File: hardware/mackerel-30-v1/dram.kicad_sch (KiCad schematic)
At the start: 28 parts, among them J11 Conn_02x05_Odd_Even, U13 EPM7128, U14 SIMM72, U15 74ABT245, U16 74ABT245, U17 74ABT245, U2 74ABT245

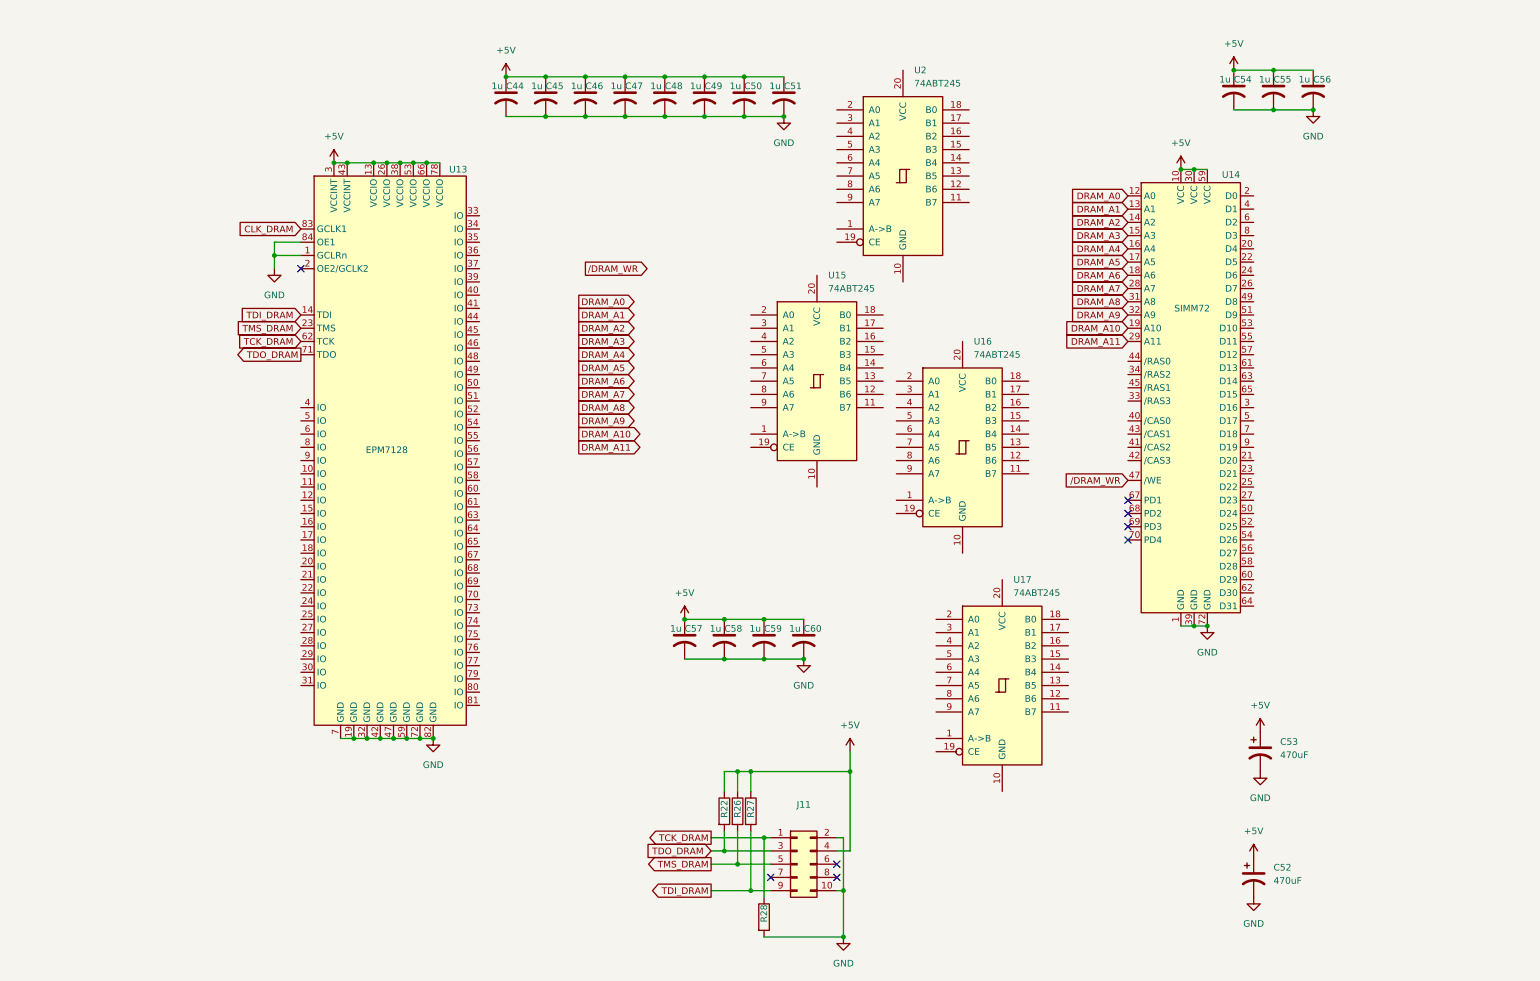
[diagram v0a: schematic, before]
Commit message: SIMM and data buffers mostly routed
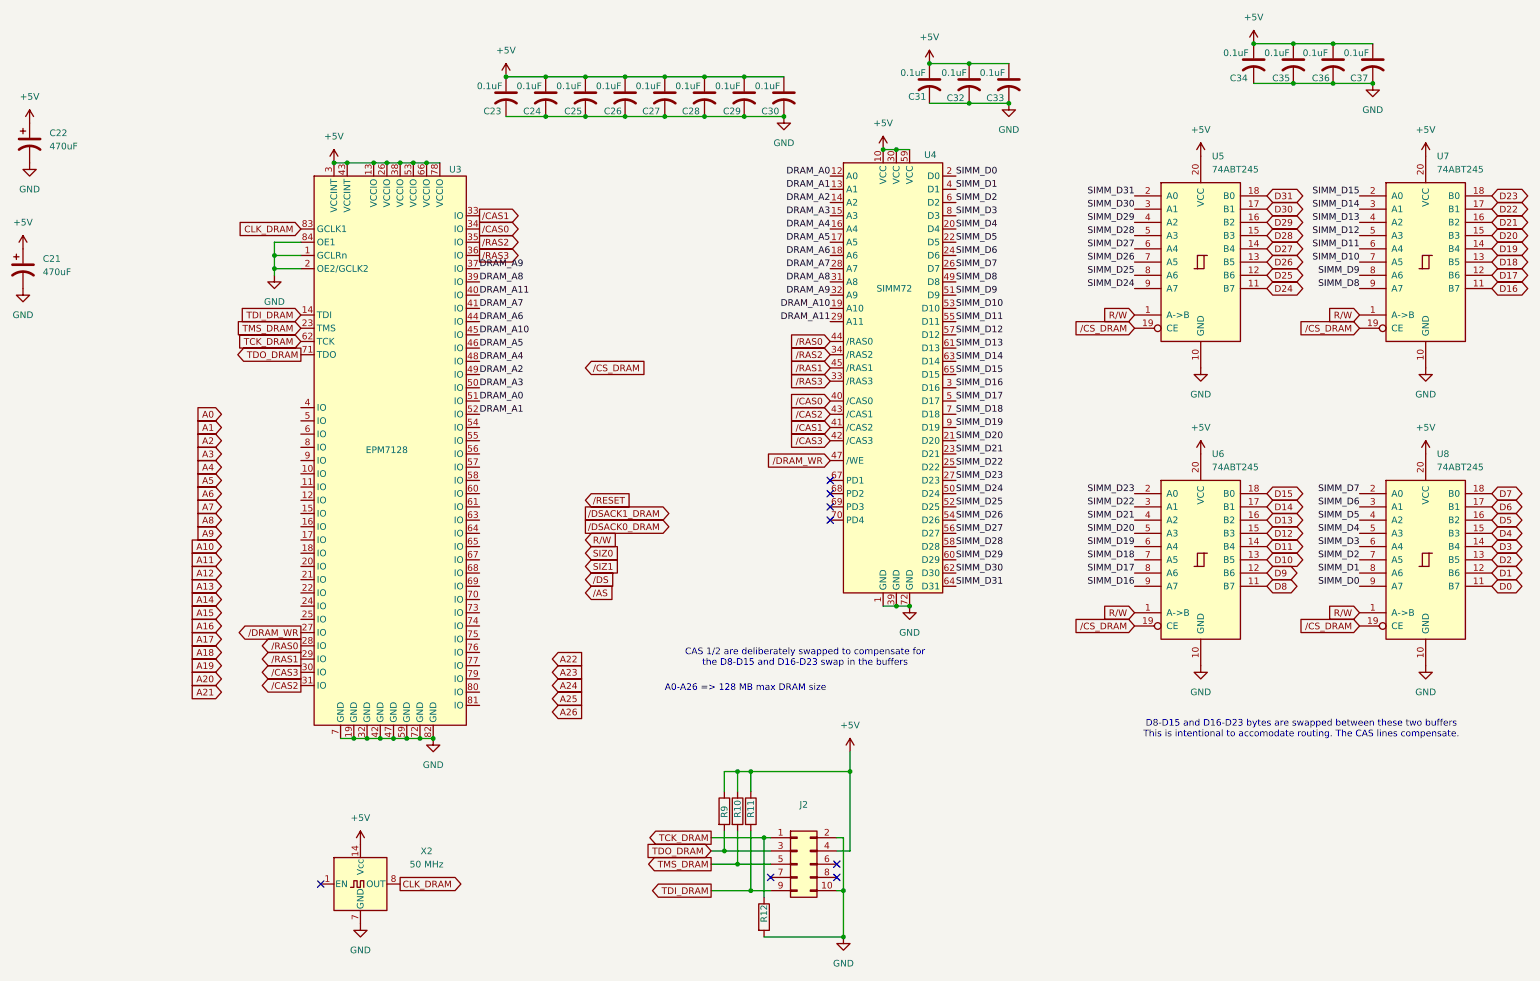
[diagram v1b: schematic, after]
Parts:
- added X2: 50 MHz, Oscillator:Oscillator_DIP-14, symbol Oscillator:CXO_DIP14
- C23: renamed from C44; value 1u -> 0.1uF; footprint Capacitor_SMD:C_0805_2012Metric_Pad1.18x1.45mm_HandSolder -> Capacitor_SMD:C_1206_3216Metric_Pad1.33x1.80mm_HandSolder
- C24: renamed from C45; value 1u -> 0.1uF; footprint Capacitor_SMD:C_0805_2012Metric_Pad1.18x1.45mm_HandSolder -> Capacitor_SMD:C_1206_3216Metric_Pad1.33x1.80mm_HandSolder
- C25: renamed from C46; value 1u -> 0.1uF; footprint Capacitor_SMD:C_0805_2012Metric_Pad1.18x1.45mm_HandSolder -> Capacitor_SMD:C_1206_3216Metric_Pad1.33x1.80mm_HandSolder
- C26: renamed from C47; value 1u -> 0.1uF; footprint Capacitor_SMD:C_0805_2012Metric_Pad1.18x1.45mm_HandSolder -> Capacitor_SMD:C_1206_3216Metric_Pad1.33x1.80mm_HandSolder
- C27: renamed from C48; value 1u -> 0.1uF; footprint Capacitor_SMD:C_0805_2012Metric_Pad1.18x1.45mm_HandSolder -> Capacitor_SMD:C_1206_3216Metric_Pad1.33x1.80mm_HandSolder
- C28: renamed from C49; value 1u -> 0.1uF; footprint Capacitor_SMD:C_0805_2012Metric_Pad1.18x1.45mm_HandSolder -> Capacitor_SMD:C_1206_3216Metric_Pad1.33x1.80mm_HandSolder
- C29: renamed from C50; value 1u -> 0.1uF; footprint Capacitor_SMD:C_0805_2012Metric_Pad1.18x1.45mm_HandSolder -> Capacitor_SMD:C_1206_3216Metric_Pad1.33x1.80mm_HandSolder
- C30: renamed from C51; value 1u -> 0.1uF; footprint Capacitor_SMD:C_0805_2012Metric_Pad1.18x1.45mm_HandSolder -> Capacitor_SMD:C_1206_3216Metric_Pad1.33x1.80mm_HandSolder
- C31: renamed from C54; value 1u -> 0.1uF; footprint Capacitor_SMD:C_0805_2012Metric_Pad1.18x1.45mm_HandSolder -> Capacitor_SMD:C_1206_3216Metric_Pad1.33x1.80mm_HandSolder
- C32: renamed from C55; value 1u -> 0.1uF; footprint Capacitor_SMD:C_0805_2012Metric_Pad1.18x1.45mm_HandSolder -> Capacitor_SMD:C_1206_3216Metric_Pad1.33x1.80mm_HandSolder
- C33: renamed from C56; value 1u -> 0.1uF; footprint Capacitor_SMD:C_0805_2012Metric_Pad1.18x1.45mm_HandSolder -> Capacitor_SMD:C_1206_3216Metric_Pad1.33x1.80mm_HandSolder
- C34: renamed from C57; value 1u -> 0.1uF; footprint Capacitor_SMD:C_0805_2012Metric_Pad1.18x1.45mm_HandSolder -> Capacitor_SMD:C_1206_3216Metric_Pad1.33x1.80mm_HandSolder
- C35: renamed from C58; value 1u -> 0.1uF; footprint Capacitor_SMD:C_0805_2012Metric_Pad1.18x1.45mm_HandSolder -> Capacitor_SMD:C_1206_3216Metric_Pad1.33x1.80mm_HandSolder
- C36: renamed from C59; value 1u -> 0.1uF; footprint Capacitor_SMD:C_0805_2012Metric_Pad1.18x1.45mm_HandSolder -> Capacitor_SMD:C_1206_3216Metric_Pad1.33x1.80mm_HandSolder
- C37: renamed from C60; value 1u -> 0.1uF; footprint Capacitor_SMD:C_0805_2012Metric_Pad1.18x1.45mm_HandSolder -> Capacitor_SMD:C_1206_3216Metric_Pad1.33x1.80mm_HandSolder
- R10: renamed from R26; footprint Resistor_THT:R_Axial_DIN0207_L6.3mm_D2.5mm_P7.62mm_Horizontal -> Resistor_SMD:R_1206_3216Metric_Pad1.30x1.75mm_HandSolder
- R11: renamed from R27; footprint Resistor_THT:R_Axial_DIN0207_L6.3mm_D2.5mm_P7.62mm_Horizontal -> Resistor_SMD:R_1206_3216Metric_Pad1.30x1.75mm_HandSolder
- R12: renamed from R28; footprint Resistor_THT:R_Axial_DIN0207_L6.3mm_D2.5mm_P7.62mm_Horizontal -> Resistor_SMD:R_1206_3216Metric_Pad1.30x1.75mm_HandSolder
- R9: renamed from R22; footprint Resistor_THT:R_Axial_DIN0207_L6.3mm_D2.5mm_P7.62mm_Horizontal -> Resistor_SMD:R_1206_3216Metric_Pad1.30x1.75mm_HandSolder
- renumbered C52 to C21, C53 to C22, J11 to J2, U13 to U3, U14 to U4, U15 to U5, U16 to U6, U2 to U7, U17 to U8
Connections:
- net +5V: now also U5.20 (VCC), U6.20 (VCC), U7.20 (VCC), U8.20 (VCC), X2.14 (Vcc)
- net CLK_DRAM: now also X2.8 (OUT)
- net DRAM_A0: now also U3.51 (IO)
- net DRAM_A1: now also U3.52 (IO)
- net DRAM_A10: now also U3.45 (IO)
- net DRAM_A11: now also U3.40 (IO)
- net DRAM_A2: now also U3.49 (IO)
- net DRAM_A3: now also U3.50 (IO)
- net DRAM_A4: now also U3.48 (IO)
- net DRAM_A5: now also U3.46 (IO)
- net DRAM_A6: now also U3.44 (IO)
- net DRAM_A7: now also U3.41 (IO)
- net DRAM_A8: now also U3.39 (IO)
- net DRAM_A9: now also U3.37 (IO)
- net GND: now also U3.2 (OE2/GCLK2), U5.10 (GND), U6.10 (GND), U7.10 (GND), U8.10 (GND), X2.7 (GND)
- net /DRAM_WR: now also U3.27 (IO)
- net R/W: now reaches U7.1 (A->B)
- net R/W: now also U5.1 (A->B), U6.1 (A->B), U8.1 (A->B)
- net D16: now reaches U7.11 (B7)
- net D17: now reaches U7.12 (B6)
- net D18: now reaches U7.13 (B5)
- net D19: now reaches U7.14 (B4)
- net D20: now reaches U7.15 (B3)
- net D21: now reaches U7.16 (B2)
- net D22: now reaches U7.17 (B1)
- net D23: now reaches U7.18 (B0)
- net /CS_DRAM: now reaches U7.19 (CE)
- net /CS_DRAM: now also U5.19 (CE), U6.19 (CE), U8.19 (CE)
- net SIMM_D15: now reaches U7.2 (A0)
- net SIMM_D15: now also U4.65 (D15)
- net SIMM_D14: now reaches U7.3 (A1)
- net SIMM_D14: now also U4.63 (D14)
- net SIMM_D13: now reaches U7.4 (A2)
- net SIMM_D13: now also U4.61 (D13)
- net SIMM_D12: now reaches U7.5 (A3)
- net SIMM_D12: now also U4.57 (D12)
- net SIMM_D11: now reaches U7.6 (A4)
- net SIMM_D11: now also U4.55 (D11)
- net SIMM_D10: now reaches U7.7 (A5)
- net SIMM_D10: now also U4.53 (D10)
- net SIMM_D9: now reaches U7.8 (A6)
- net SIMM_D9: now also U4.51 (D9)
- net SIMM_D8: now reaches U7.9 (A7)
- net SIMM_D8: now also U4.49 (D8)
- net D8: now reaches U6.11 (B7)
- net D9: now reaches U6.12 (B6)
- net D10: now reaches U6.13 (B5)
- net D11: now reaches U6.14 (B4)
- net D12: now reaches U6.15 (B3)
- net D13: now reaches U6.16 (B2)
- net D14: now reaches U6.17 (B1)
- net D15: now reaches U6.18 (B0)
- net SIMM_D23: now reaches U6.2 (A0)
- net SIMM_D23: now also U4.27 (D23)
- net SIMM_D22: now reaches U6.3 (A1)
- net SIMM_D22: now also U4.25 (D22)
- net SIMM_D21: now reaches U6.4 (A2)
- net SIMM_D21: now also U4.23 (D21)
- net SIMM_D20: now reaches U6.5 (A3)
- net SIMM_D20: now also U4.21 (D20)
- net SIMM_D19: now reaches U6.6 (A4)
- net SIMM_D19: now also U4.9 (D19)
- net SIMM_D18: now reaches U6.7 (A5)
- net SIMM_D18: now also U4.7 (D18)
- net SIMM_D17: now reaches U6.8 (A6)
- net SIMM_D17: now also U4.5 (D17)
- net SIMM_D16: now reaches U6.9 (A7)
- net SIMM_D16: now also U4.3 (D16)
- net SIMM_D0: now reaches U4.2 (D0)
- net SIMM_D0: now also U8.9 (A7)
- net SIMM_D4: now reaches U4.20 (D4)
- net SIMM_D4: now also U8.5 (A3)
- net SIMM_D5: now reaches U4.22 (D5)
- net SIMM_D5: now also U8.4 (A2)
- net SIMM_D6: now reaches U4.24 (D6)
- net SIMM_D6: now also U8.3 (A1)
- net SIMM_D7: now reaches U4.26 (D7)
- net SIMM_D7: now also U8.2 (A0)
- net /RAS3: now reaches U4.33 (/RAS3)
- net /RAS3: now also U3.36 (IO)
- net /RAS2: now reaches U4.34 (/RAS2)
- net /RAS2: now also U3.35 (IO)
- net SIMM_D1: now reaches U4.4 (D1)
- net SIMM_D1: now also U8.8 (A6)
- net /CAS0: now reaches U4.40 (/CAS0)
- net /CAS0: now also U3.34 (IO)
- net /CAS1: now reaches U4.41 (/CAS2)
- net /CAS1: now also U3.33 (IO)
- net /CAS3: now reaches U4.42 (/CAS3)
- net /CAS3: now also U3.30 (IO)
- net /CAS2: now reaches U4.43 (/CAS1)
- net /CAS2: now also U3.31 (IO)
- net /RAS0: now reaches U4.44 (/RAS0)
- net /RAS0: now also U3.28 (IO)
- net /RAS1: now reaches U4.45 (/RAS1)
- net /RAS1: now also U3.29 (IO)
- net SIMM_D24: now reaches U4.50 (D24)
- net SIMM_D24: now also U5.9 (A7)
- net SIMM_D25: now reaches U4.52 (D25)
- net SIMM_D25: now also U5.8 (A6)
- net SIMM_D26: now reaches U4.54 (D26)
- net SIMM_D26: now also U5.7 (A5)
- net SIMM_D27: now reaches U4.56 (D27)
- net SIMM_D27: now also U5.6 (A4)
- net SIMM_D28: now reaches U4.58 (D28)
- net SIMM_D28: now also U5.5 (A3)
- net SIMM_D2: now reaches U4.6 (D2)
- net SIMM_D2: now also U8.7 (A5)
- net SIMM_D29: now reaches U4.60 (D29)
- net SIMM_D29: now also U5.4 (A2)
- net SIMM_D30: now reaches U4.62 (D30)
- net SIMM_D30: now also U5.3 (A1)
- net SIMM_D31: now reaches U4.64 (D31)
- net SIMM_D31: now also U5.2 (A0)
- net SIMM_D3: now reaches U4.8 (D3)
- net SIMM_D3: now also U8.6 (A4)
- net D24: now reaches U5.11 (B7)
- net D25: now reaches U5.12 (B6)
- net D26: now reaches U5.13 (B5)
- net D27: now reaches U5.14 (B4)
- net D28: now reaches U5.15 (B3)
- net D29: now reaches U5.16 (B2)
- net D30: now reaches U5.17 (B1)
- net D31: now reaches U5.18 (B0)
- net D0: now reaches U8.11 (B7)
- net D1: now reaches U8.12 (B6)
- net D2: now reaches U8.13 (B5)
- net D3: now reaches U8.14 (B4)
- net D4: now reaches U8.15 (B3)
- net D5: now reaches U8.16 (B2)
- net D6: now reaches U8.17 (B1)
- net D7: now reaches U8.18 (B0)
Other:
- note added: "A0-A26 => 128 MB max DRAM size"
- note added: "CAS 1/2 are deliberately swapped to compensate for the D8-D15 and D16-D23 swap in the buffers"
- note added: "D8-D15 and D16-D23 bytes are swapped between these two buffers This is intentional to accomodate routing. The CAS lines compensate."
- moved on the sheet: C21, C22, C31, C32, C33, C34, C35, C36, C37, U4, U5, U6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
